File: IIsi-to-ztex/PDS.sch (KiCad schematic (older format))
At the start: 31 parts, among them J2 650906-5, U1 SN74CB3T3245PWR, U10 SN74CB3T3245PWR, U11 SN74CB3T3245PWR, U13 SN74CB3T3245PWR, U14 SN74LV1T125DCKR, U2 SN74CB3T3245PWR, U3 SN74CB3T3245PWR, U4 SN74CB3T3245PWR, U5 SN74CB3T3245PWR, U6 SN74CB3T3245PWR, U7 SN74CB3T3245PWR, U8 SN74CB3T3245PWR, U9 SN74CB3T3245PWR

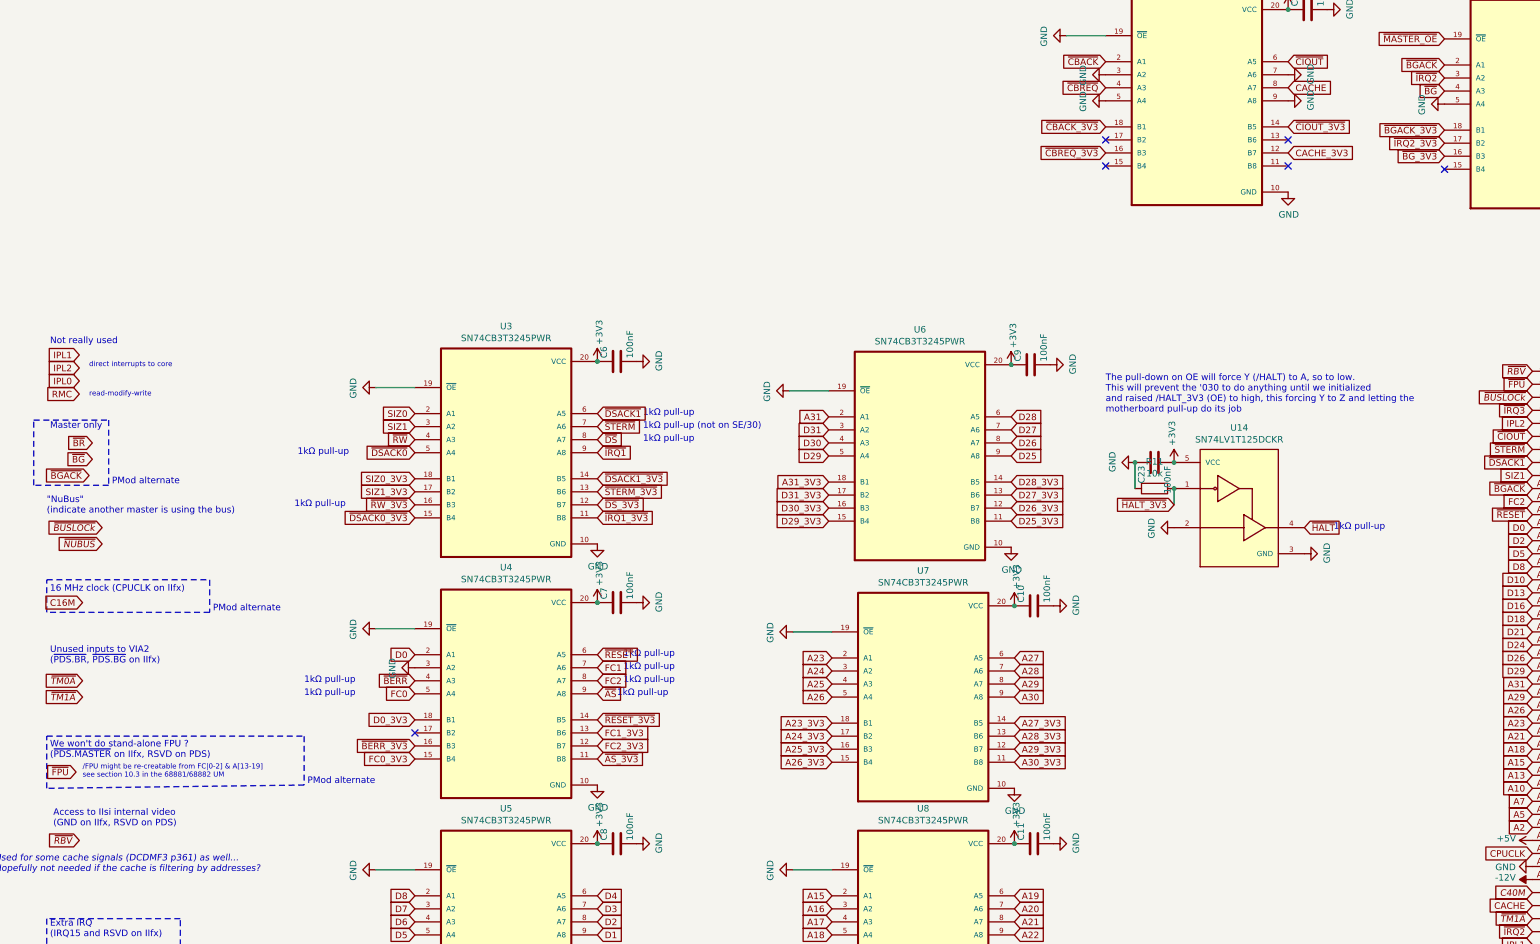
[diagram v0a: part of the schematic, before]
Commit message: connect rbv to last pmod pin
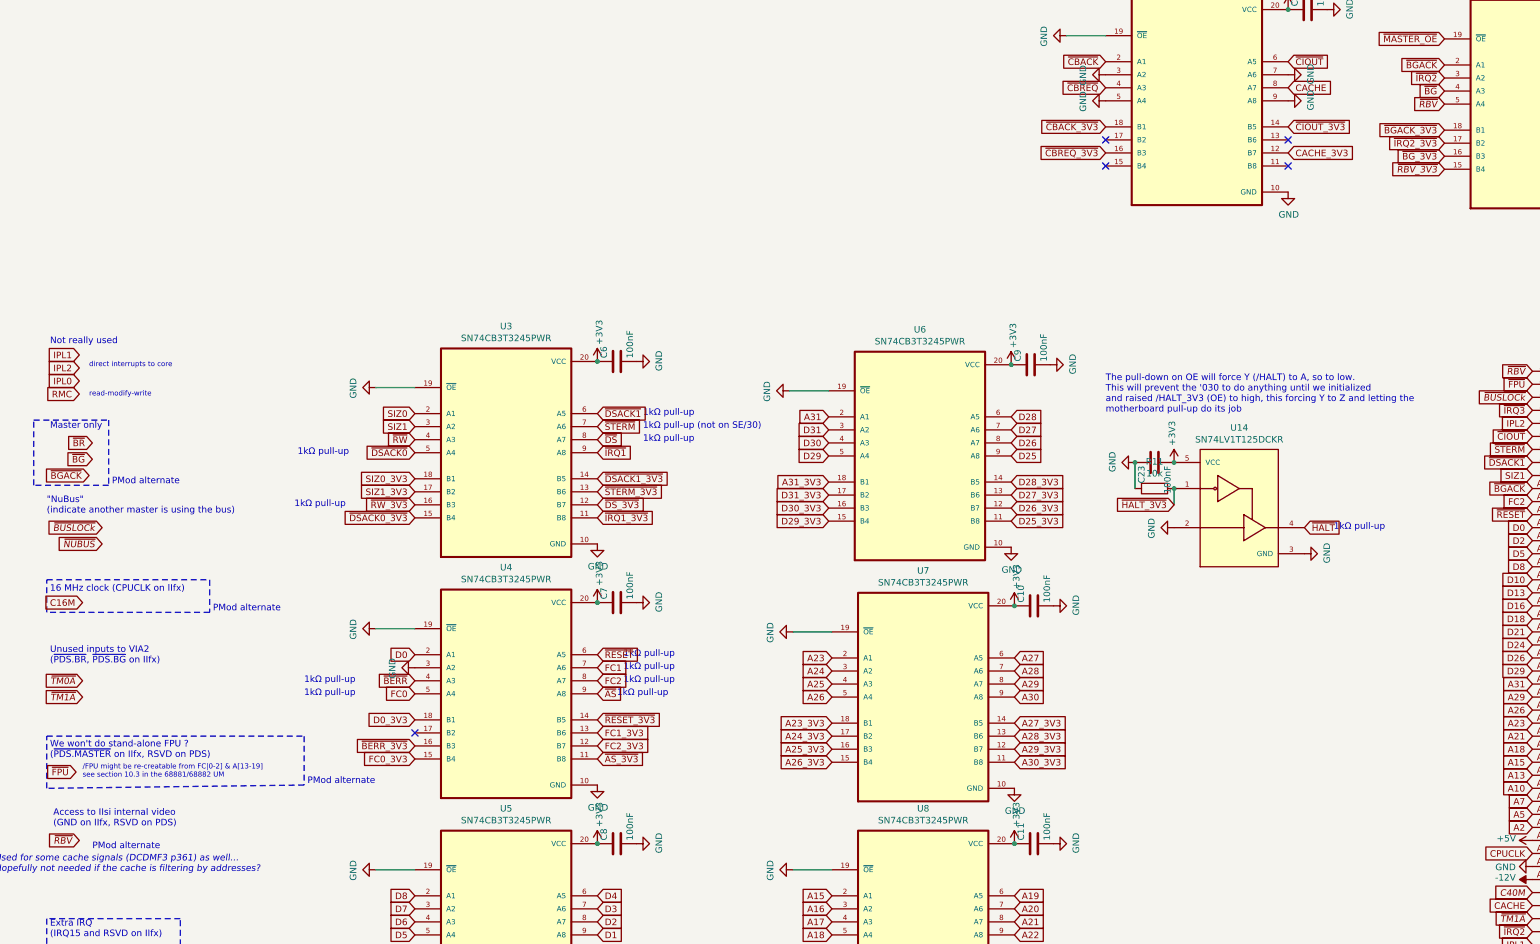
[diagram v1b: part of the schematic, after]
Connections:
- net GND: no longer U13.5 (A4)
- net ~RBV: now also U13.5 (A4)
- net ~RBV_3V3: now reaches U13.15 (B4)
- no-connect marks 6 -> 5
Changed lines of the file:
@@
 Text GLabel 10375 -425 2    50   Input ~ 0
 ~FPU_3V3
-NoConn ~ 8975 -425
 $Comp
 L Device:R R14
@@
 Text GLabel 10375 -625 2    50   Input ~ 0
 ~IRQ3_3V3
-$Comp
-L power:GND #PWR0142
-U 1 1 646A7E11
-P 8975 -925
-F 0 "#PWR0142" H 8975 -1175 50  0001 C CNN
-F 1 "GND" H 8980 -1098 50  0000 C CNN
-F 2 "" H 8975 -925 50  0001 C CNN
-F 3 "" H 8975 -925 50  0001 C CNN
-	1    8975 -925
-	0    1    1    0
-$EndComp
 Text GLabel 8975 -1125 0    50   Input ~ 0
 ~IRQ2
@@
 Text Notes 8650 -2050 0    50   ~ 0
 When ~MASTER_OE~ is low, this is enabled and various signals for Master & the extra clock (primary clock on IIfx) are available to the FPGA.\nWhen ~MASTER_OE~ is high, this is high-Z and the PMod can be used instead
+Text Notes -1400 4800 0    50   ~ 0
+PMod alternate
+Text GLabel 8975 -925 0    50   Input Italic 0
+~RBV
+Text GLabel 8975 -425 0    50   Input Italic 0
+~RBV_3V3
 $EndSCHEMATC

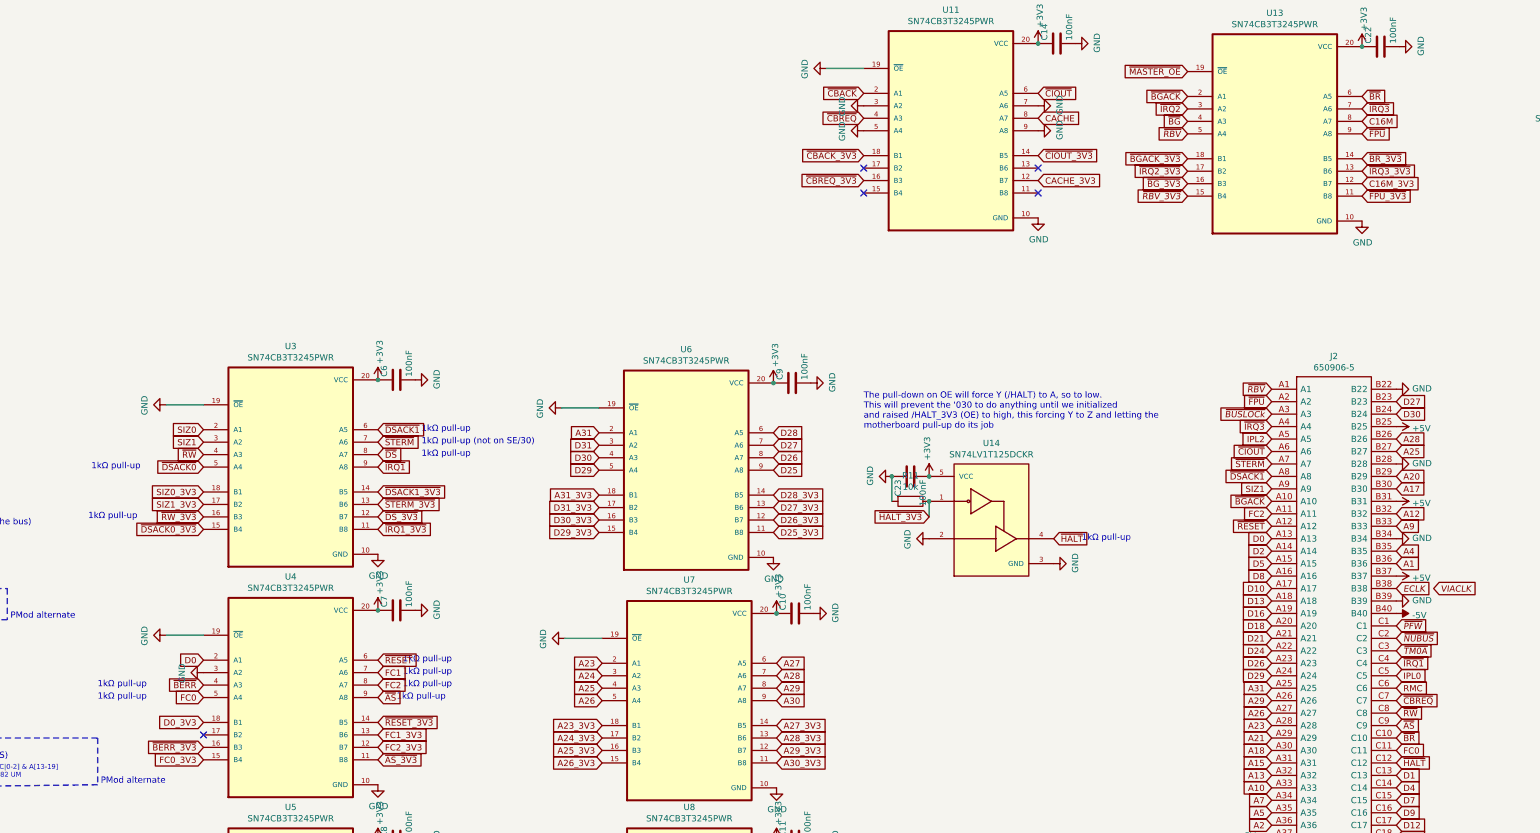
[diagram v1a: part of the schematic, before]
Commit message: some pull-(up,down)s
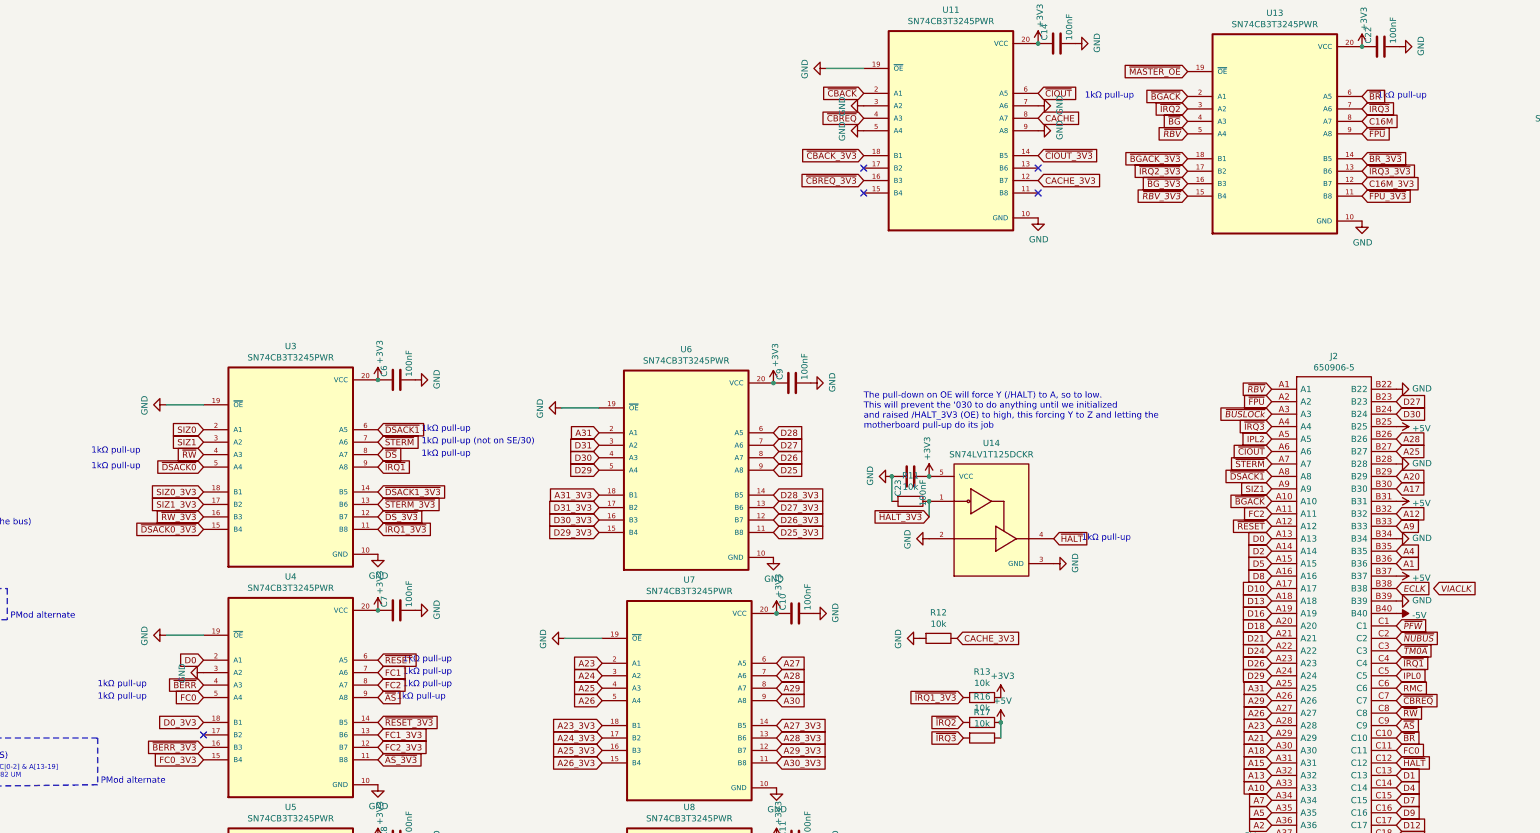
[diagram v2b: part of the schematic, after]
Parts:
- added R12, R13, R16, R17: 10k, Resistor_SMD:R_0603_1608Metric, symbol Device:R
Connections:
- net +3V3: now also R13.1
- net +5V: now also R16.1, R17.1
- net CACHE_3V3: now also R12.1
- net GND: now also R12.2
- net ~IRQ1_3V3: now also R13.2
- net ~IRQ2: now also R16.2
- net ~IRQ3: now also R17.2
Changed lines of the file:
@@
 Text Notes 2825 1475 0    50   ~ 0
  1kΩ pull-up
-Text Notes 2825 1575 0    50   ~ 0
- 1kΩ pull-up (not on SE/30)
 Text Notes 2825 1675 0    50   ~ 0
  1kΩ pull-up
@@
 Text Notes 225  3625 0    50   ~ 0
  1kΩ pull-up
-Text Notes 150  2175 0    50   ~ 0
+Text Notes 175  1650 0    50   ~ 0
  1kΩ pull-up
 Text Notes 2625 3625 0    50   ~ 0
@@
 Text GLabel 8975 -425 0    50   Input Italic 0
 ~RBV_3V3
+Text GLabel 7125 3125 2    50   Input ~ 0
+CACHE_3V3
+$Comp
+L Device:R R12
+U 1 1 64A08964
+P 6975 3125
+F 0 "R12" V 6768 3125 50  0000 C CNN
+F 1 "10k" V 6859 3125 50  0000 C CNN
+F 2 "Resistor_SMD:R_0603_1608Metric" V 6905 3125 50  0001 C CNN
+F 3 "~" H 6975 3125 50  0001 C CNN
+F 4 "0603WAF1002T5E" V 6975 3125 50  0001 C CNN "MPN"
+	1    6975 3125
+	0    1    1    0
+$EndComp
+$Comp
+L power:GND #PWR0142
+U 1 1 64A0740C
+P 6825 3125
+F 0 "#PWR0142" H 6825 2875 50  0001 C CNN
+F 1 "GND" H 6830 2952 50  0000 C CNN
+F 2 "" H 6825 3125 50  0001 C CNN
+F 3 "" H 6825 3125 50  0001 C CNN
+	1    6825 3125
+	0    1    1    0
+$EndComp
+Text Notes 2825 1575 0    50   ~ 0
+ 1kΩ pull-up (not on SE/30)
+Text Notes 10500 -1200 0    50   ~ 0
+ 1kΩ pull-up
+Text Notes 8150 -1200 0    50   ~ 0
+ 1kΩ pull-up
+Text GLabel 7175 3800 0    50   Input ~ 0
+~IRQ2
+Text GLabel 7175 3925 0    50   Input ~ 0
+~IRQ3
+$Comp
+L Device:R R13
+U 1 1 64AB2C77
+P 7325 3600
+F 0 "R13" V 7118 3600 50  0000 C CNN
+F 1 "10k" V 7209 3600 50  0000 C CNN
+F 2 "Resistor_SMD:R_0603_1608Metric" V 7255 3600 50  0001 C CNN
+F 3 "~" H 7325 3600 50  0001 C CNN
+F 4 "0603WAF1002T5E" V 7325 3600 50  0001 C CNN "MPN"
+	1    7325 3600
+	0    1    1    0
+$EndComp
+$Comp
+L Device:R R16
+U 1 1 64AB32C6
+P 7325 3800
+F 0 "R16" V 7118 3800 50  0000 C CNN
+F 1 "10k" V 7209 3800 50  0000 C CNN
+F 2 "Resistor_SMD:R_0603_1608Metric" V 7255 3800 50  0001 C CNN
+F 3 "~" H 7325 3800 50  0001 C CNN
+F 4 "0603WAF1002T5E" V 7325 3800 50  0001 C CNN "MPN"
+	1    7325 3800
+	0    1    1    0
+$EndComp
+$Comp
+L Device:R R17
+U 1 1 64AB3785
+P 7325 3925
+F 0 "R17" V 7118 3925 50  0000 C CNN
+F 1 "10k" V 7209 3925 50  0000 C CNN
+F 2 "Resistor_SMD:R_0603_1608Metric" V 7255 3925 50  0001 C CNN
+F 3 "~" H 7325 3925 50  0001 C CNN
+F 4 "0603WAF1002T5E" V 7325 3925 50  0001 C CNN "MPN"
+	1    7325 3925
+	0    1    1    0
+$EndComp
+Wire Wire Line
+	7475 3925 7475 3800
+$Comp
+L power:+5V #PWR0146
+U 1 1 64AB7123
+P 7475 3800
+F 0 "#PWR0146" H 7475 3650 50  0001 C CNN
+F 1 "+5V" H 7490 3973 50  0000 C CNN
+F 2 "" H 7475 3800 50  0001 C CNN
+F 3 "" H 7475 3800 50  0001 C CNN
+	1    7475 3800
+	1    0    0    -1
+$EndComp
+Connection ~ 7475 3800
+Text GLabel 7175 3600 0    50   Input ~ 0
+~IRQ1_3V3
+$Comp
+L power:+3V3 #PWR?
+U 1 1 64AE14D2
+P 7475 3600
+F 0 "#PWR?" H 7475 3450 50  0001 C CNN
+F 1 "+3V3" H 7490 3773 50  0000 C CNN
+F 2 "" H 7475 3600 50  0001 C CNN
+F 3 "" H 7475 3600 50  0001 C CNN
+	1    7475 3600
+	1    0    0    -1
+$EndComp
 $EndSCHEMATC
